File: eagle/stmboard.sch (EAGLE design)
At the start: 23 parts, among them IC1 LD1117S33TR

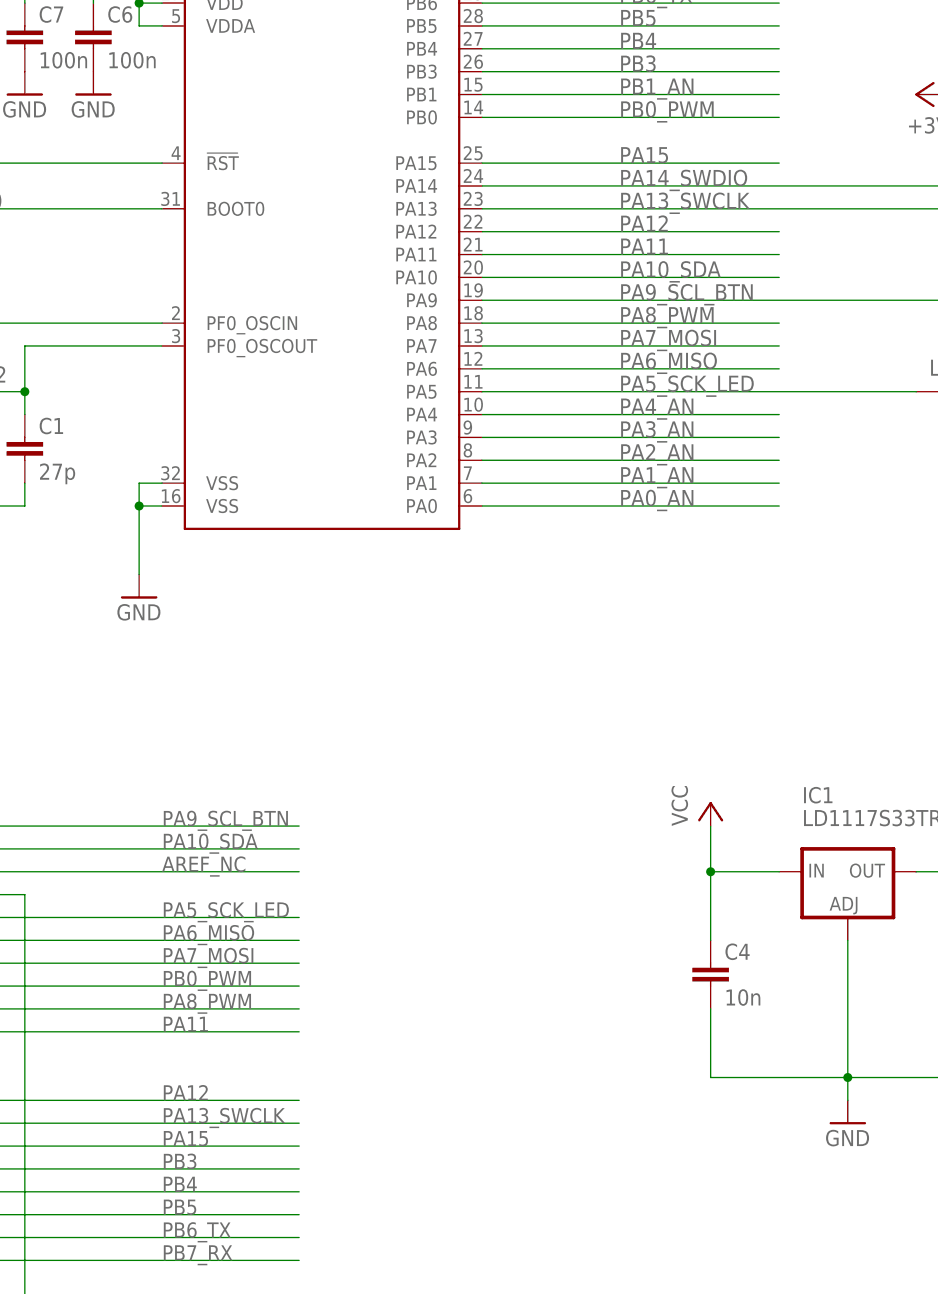
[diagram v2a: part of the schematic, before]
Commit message: fixed SWDIO/SWCLK signal names
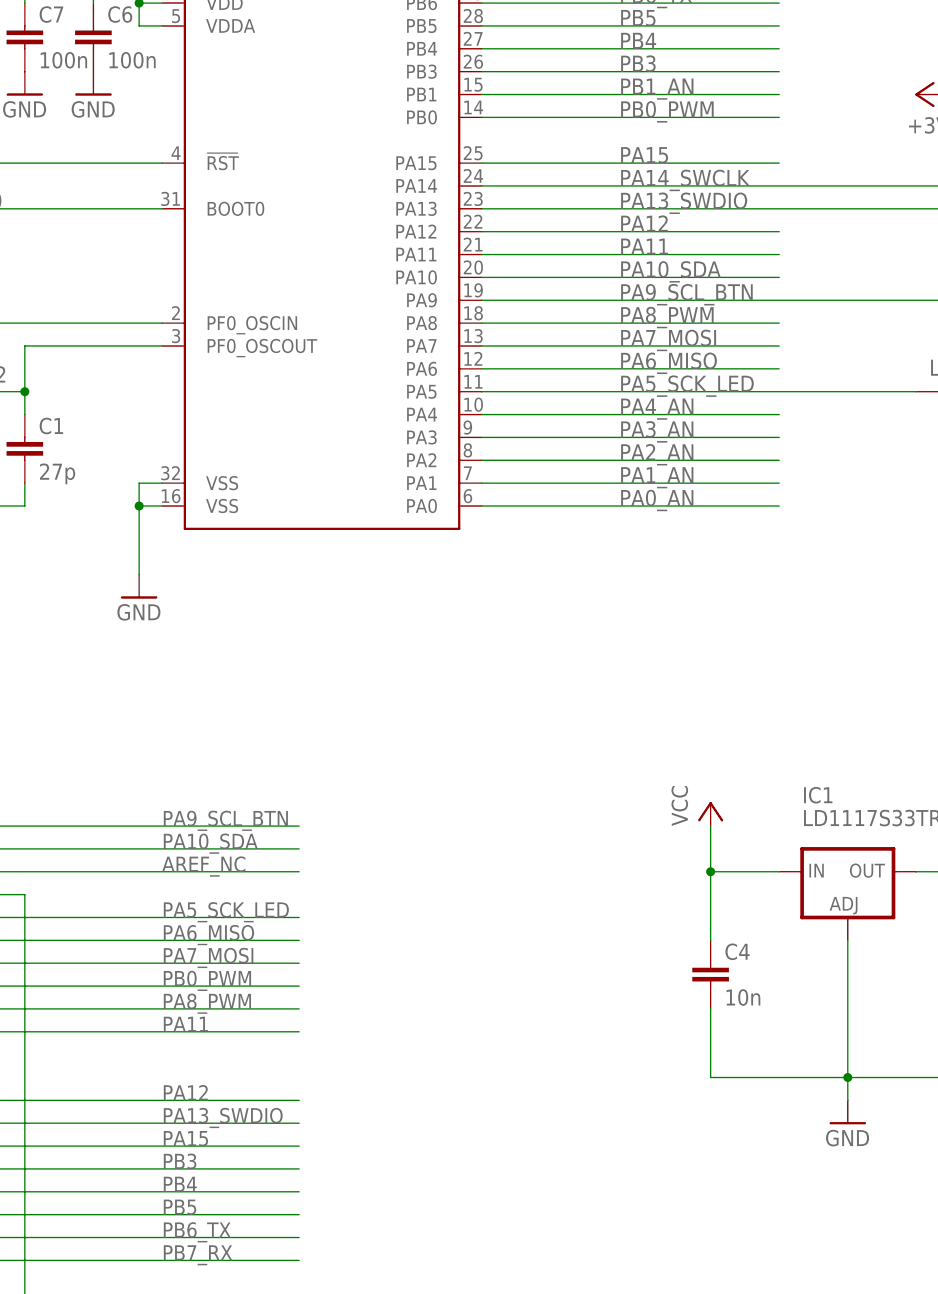
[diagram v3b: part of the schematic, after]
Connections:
- net PA13_SWCLK renamed PA13_SWDIO
- net PA14_SWDIO renamed PA14_SWCLK
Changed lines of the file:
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@@
 </segment>
 </net>
-<net name="PA14_SWDIO" class="0">
+<net name="PA14_SWCLK" class="0">
 <segment>
 <pinref part="U$1" gate="G$1" pin="PA14"/>
@@
 <wire x1="429.26" y1="101.6" x2="462.28" y2="101.6" width="0.1524" layer="91"/>
 <label x="444.5" y="101.6" size="1.778" layer="95"/>
-</segment>
-</net>
-<net name="PA13_SWCLK" class="0">
-<segment>
-<pinref part="JP5" gate="A" pin="7"/>
-<wire x1="370.84" y1="-5.08" x2="408.94" y2="-5.08" width="0.1524" layer="91"/>
-<label x="393.7" y="-5.08" size="1.6764" layer="95"/>
-</segment>
-<segment>
-<pinref part="U$1" gate="G$1" pin="PA13"/>
-<pinref part="JP8" gate="A" pin="4"/>
-<wire x1="429.26" y1="96.52" x2="495.3" y2="96.52" width="0.1524" layer="91"/>
-<wire x1="495.3" y1="96.52" x2="495.3" y2="116.84" width="0.1524" layer="91"/>
-<label x="444.5" y="96.52" size="1.778" layer="95"/>
 </segment>
 </net>
@@
 </segment>
 </net>
+<net name="PA13_SWDIO" class="0">
+<segment>
+<pinref part="U$1" gate="G$1" pin="PA13"/>
+<pinref part="JP8" gate="A" pin="4"/>
+<wire x1="429.26" y1="96.52" x2="495.3" y2="96.52" width="0.1524" layer="91"/>
+<wire x1="495.3" y1="96.52" x2="495.3" y2="116.84" width="0.1524" layer="91"/>
+<label x="444.5" y="96.52" size="1.778" layer="95"/>
+</segment>
+<segment>
+<pinref part="JP5" gate="A" pin="7"/>
+<wire x1="370.84" y1="-5.08" x2="408.94" y2="-5.08" width="0.1524" layer="91"/>
+<label x="393.7" y="-5.08" size="1.6764" layer="95"/>
+</segment>
+</net>

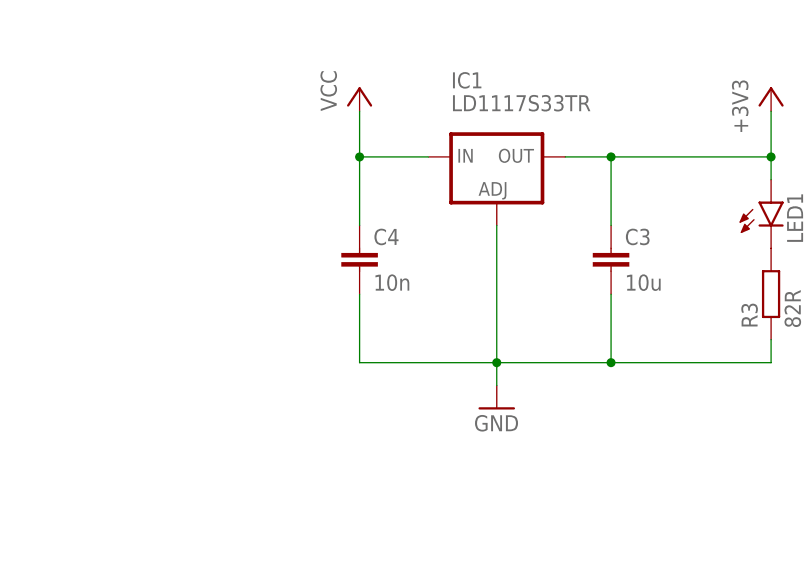
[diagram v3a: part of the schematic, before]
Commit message: fixed value labels on brd
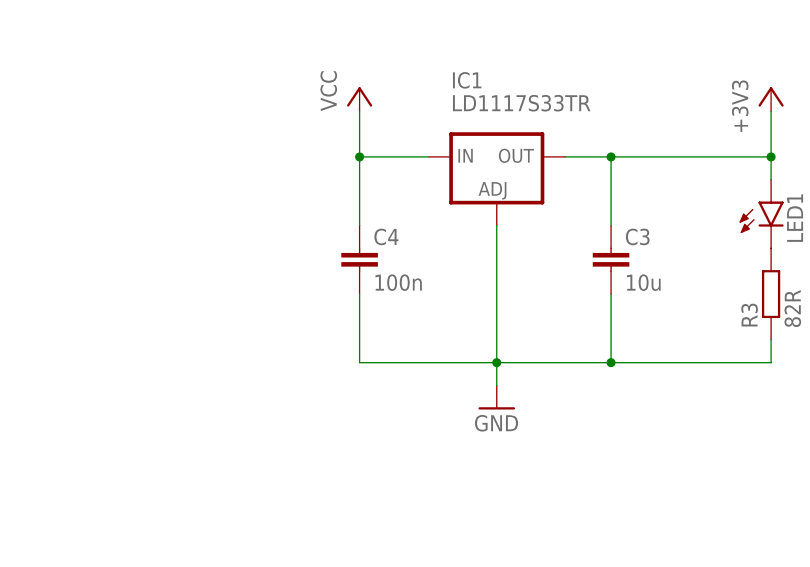
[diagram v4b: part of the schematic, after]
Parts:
- C4: value 10n -> 100n
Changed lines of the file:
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@@
 <part name="GND3" library="supply1" deviceset="GND" device=""/>
 <part name="C3" library="rcl" deviceset="C-EU" device="C1206K" value="10u"/>
-<part name="C4" library="rcl" deviceset="C-EU" device="C1206K" value="10n"/>
+<part name="C4" library="rcl" deviceset="C-EU" device="C1206K" value="100n"/>
 <part name="+3V1" library="supply1" deviceset="+3V3" device=""/>
 <part name="P+1" library="supply1" deviceset="VCC" device=""/>
